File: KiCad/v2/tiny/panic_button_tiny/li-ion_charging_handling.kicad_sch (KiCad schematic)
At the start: 2 parts, among them U6 TP4056-42-ESOP8, U7 DW01A

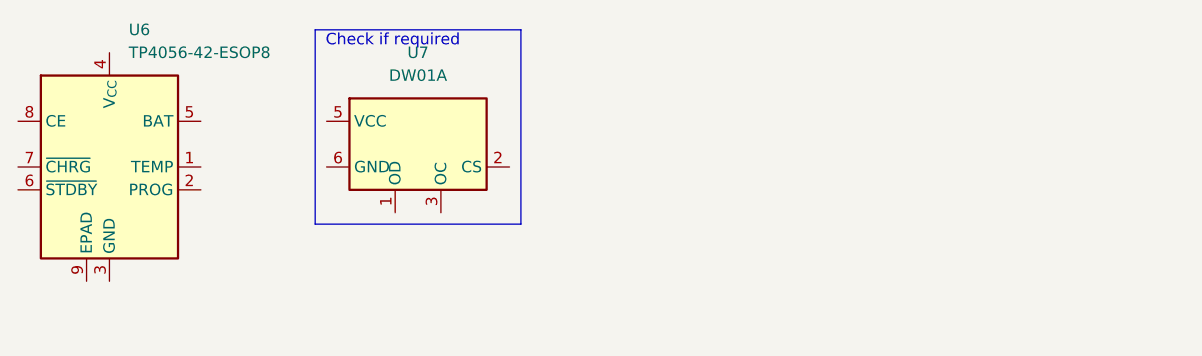
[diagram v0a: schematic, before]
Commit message: [UPDATE] the KiCad schematic to contain some of the updated designs for the circuit
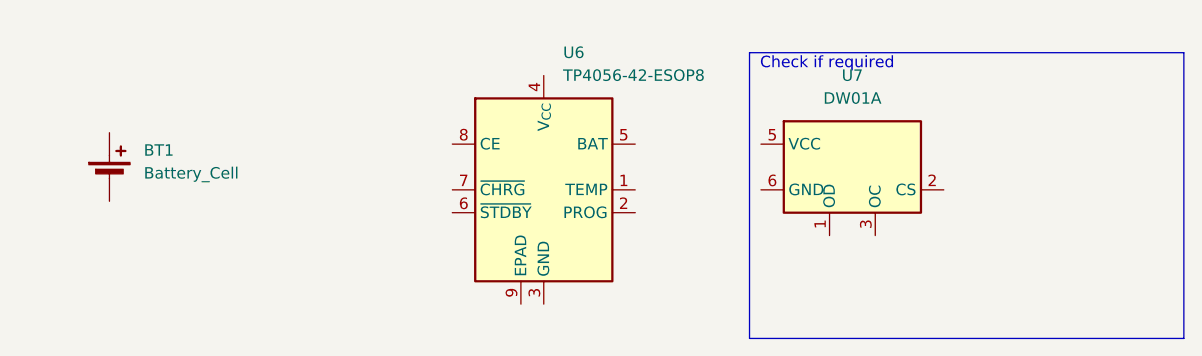
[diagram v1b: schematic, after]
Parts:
- added BT1: Battery_Cell, Connector_JST:JST_J2100_S06B-J21DK-GGXR_2x03_P2.50mm_Horizontal, symbol Device:Battery_Cell
- U7: footprint (none) -> Package_TO_SOT_SMD:SOT-23-6
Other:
- moved on the sheet: U6, U7
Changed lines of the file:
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@@
 	(paper "A4")
 	(rectangle
-		(start 55.88 15.24)
-		(end 78.74 36.83)
+		(start 104.14 17.78)
+		(end 152.4 49.53)
 		(stroke
 			(width 0)
@@
 	(text "Check if required"
 		(exclude_from_sim no)
-		(at 64.516 16.51 0)
+		(at 112.776 19.05 0)
 		(effects
 			(font
@@
 	(symbol
 		(lib_id "Battery_Management:DW01A")
-		(at 67.31 27.94 0)
+		(at 115.57 30.48 0)
 		(unit 1)
 		(body_style 1)
@@
 		(fields_autoplaced yes)
 		(property "Reference" "U7"
-			(at 67.31 17.78 0)
+			(at 115.57 20.32 0)
 			(show_name no)
 			(do_not_autoplace no)
@@
 		)
 		(property "Value" "DW01A"
-			(at 67.31 20.32 0)
-			(show_name no)
-			(do_not_autoplace no)
-			(effects
-				(font
-					(size 1.27 1.27)
-				)
-			)
-		)
-		(property "Footprint" ""
-			(at 67.31 27.94 0)
+			(at 115.57 22.86 0)
+			(show_name no)
+			(do_not_autoplace no)
+			(effects
+				(font
+					(size 1.27 1.27)
+				)
+			)
+		)
+		(property "Footprint" "Package_TO_SOT_SMD:SOT-23-6"
+			(at 115.57 30.48 0)
 			(hide yes)
 			(show_name no)
@@
 		)
 		(property "Datasheet" "https://hmsemi.com/downfile/DW01A.PDF"
-			(at 67.31 27.94 0)
+			(at 115.57 30.48 0)
 			(hide yes)
 			(show_name no)
@@
 		)
 		(property "Description" "Overcharge, overcurrent and overdischarge protection IC for single cell lithium-ion/polymer battery"
-			(at 67.564 26.416 0)
+			(at 115.824 28.956 0)
 			(hide yes)
 			(show_name no)
@@
 	)
 	(symbol
+		(lib_id "Device:Battery_Cell")
+		(at 33.02 31.75 0)
+		(unit 1)
+		(body_style 1)
+		(exclude_from_sim no)
+		(in_bom yes)
+		(on_board yes)
+		(in_pos_files yes)
+		(dnp no)
+		(fields_autoplaced yes)
+		(property "Reference" "BT1"
+			(at 36.83 28.6384 0)
+			(show_name no)
+			(do_not_autoplace no)
+			(effects
+				(font
+					(size 1.27 1.27)
+				)
+				(justify left)
+			)
+		)
+		(property "Value" "Battery_Cell"
+			(at 36.83 31.1784 0)
+			(show_name no)
+			(do_not_autoplace no)
+			(effects
+				(font
+					(size 1.27 1.27)
+				)
+				(justify left)
+			)
+		)
+		(property "Footprint" "Connector_JST:JST_J2100_S06B-J21DK-GGXR_2x03_P2.50mm_Horizontal"
+			(at 33.02 30.226 90)
+			(hide yes)
+			(show_name no)
+			(do_not_autoplace no)
+			(effects
+				(font
+					(size 1.27 1.27)
+				)
+			)
+		)
+		(property "Datasheet" ""
+			(at 33.02 30.226 90)
+			(hide yes)
+			(show_name no)
+			(do_not_autoplace no)
+			(effects
+				(font
+					(size 1.27 1.27)
+				)
+			)
+		)
+		(property "Description" "Single-cell battery"
+			(at 33.02 31.75 0)
+			(hide yes)
+			(show_name no)
+			(do_not_autoplace no)
+			(effects
+				(font
+					(size 1.27 1.27)
+				)
+			)
+		)
+		(property "Sim.Device" "V"
+			(at 33.02 31.75 0)
+			(hide yes)
+			(show_name no)
+			(do_not_autoplace no)
+			(effects
+				(font
+					(size 1.27 1.27)
+				)
+			)
+		)
+		(property "Sim.Type" "DC"
+			(at 33.02 31.75 0)
+			(hide yes)
+			(show_name no)
+			(do_not_autoplace no)
+			(effects
+				(font
+					(size 1.27 1.27)
+				)
+			)
+		)
+		(property "Sim.Pins" "1=+ 2=-"
+			(at 33.02 31.75 0)
+			(hide yes)
+			(show_name no)
+			(do_not_autoplace no)
+			(effects
+				(font
+					(size 1.27 1.27)
+				)
+			)
+		)
+		(pin "1"
+		)
+		(pin "2"
+		)
+		(instances
+			(project "panic_button_tiny"
+				(path "/c4eb92e9-b42f-4db0-b1d9-0ef70f7ca601/bf7d15b7-3a35-46fb-a5a6-5ea810f2dc2c/4988fc48-ac14-475f-a329-fd119eb80de7"
+					(reference "BT1")
+					(unit 1)
+				)
+			)
+		)
+	)
+	(symbol
 		(lib_id "Battery_Management:TP4056-42-ESOP8")
-		(at 33.02 30.48 0)
+		(at 81.28 33.02 0)
 		(unit 1)
 		(body_style 1)
@@
 		(fields_autoplaced yes)
 		(property "Reference" "U6"
-			(at 35.1633 15.24 0)
+			(at 83.4233 17.78 0)
 			(show_name no)
 			(do_not_autoplace no)
@@
 		)
 		(property "Value" "TP4056-42-ESOP8"
-			(at 35.1633 17.78 0)
+			(at 83.4233 20.32 0)
 			(show_name no)
 			(do_not_autoplace no)
@@
 		)
 		(property "Footprint" "Package_SO:SOIC-8-1EP_3.9x4.9mm_P1.27mm_EP2.41x3.3mm_ThermalVias"
-			(at 33.528 53.34 0)
+			(at 81.788 55.88 0)
 			(hide yes)
 			(show_name no)
@@
 		)
 		(property "Datasheet" "https://www.lcsc.com/datasheet/lcsc_datasheet_2410121619_TOPPOWER-Nanjing-Extension-Microelectronics-TP4056-42-ESOP8_C16581.pdf"
-			(at 33.02 55.88 0)
+			(at 81.28 58.42 0)
 			(hide yes)
 			(show_name no)
@@
 		)
 		(property "Description" "1A Standalone Linear Li-ion/LiPo single-cell battery charger, 4.2V ±1% charge voltage, VCC = 4.0..8.0V, SOIC-8 (SOP-8)"
-			(at 33.528 50.8 0)
-			(hide yes)
-			(show_name no)
+			(at 81.788 53.34 0)
+			(hide yes)
+			(show_name no)

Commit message: [UPDATE] some of the pcb design and layout
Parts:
- BT1: footprint Connector_JST:JST_J2100_S06B-J21DK-GGXR_2x03_P2.50mm_Horizontal -> Connector_JST:JST_EH_S2B-EH_1x02_P2.50mm_Horizontal
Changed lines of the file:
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@@
 			)
 		)
-		(property "Footprint" "Connector_JST:JST_J2100_S06B-J21DK-GGXR_2x03_P2.50mm_Horizontal"
+		(property "Footprint" "Connector_JST:JST_EH_S2B-EH_1x02_P2.50mm_Horizontal"
 			(at 33.02 30.226 90)
 			(hide yes)

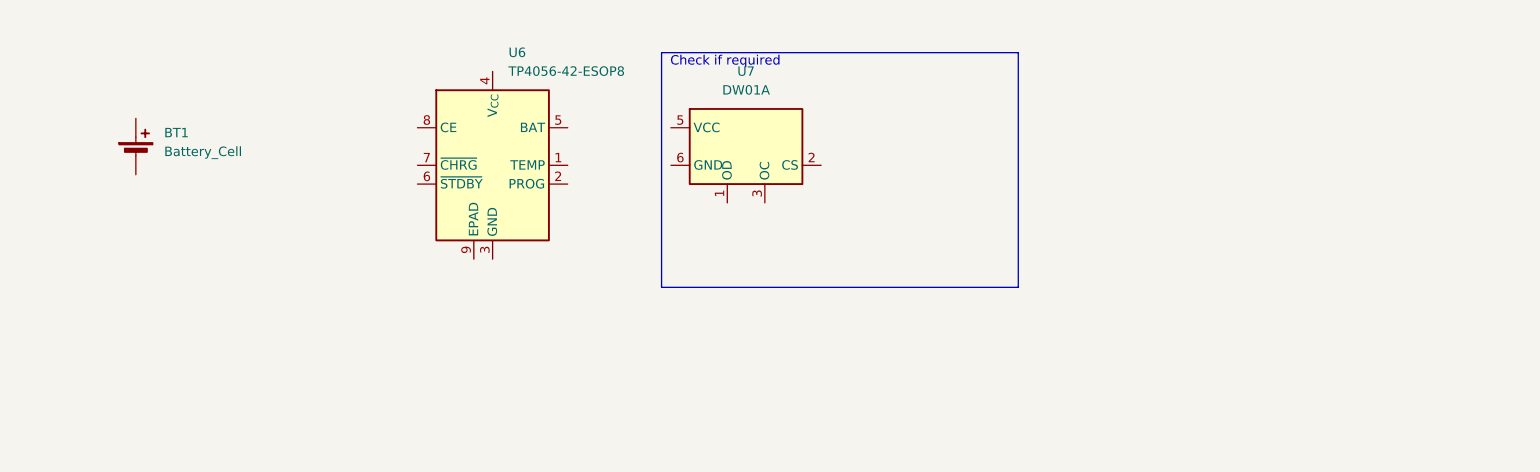
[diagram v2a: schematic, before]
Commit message: [UPDATE] connections in the circuit schematic
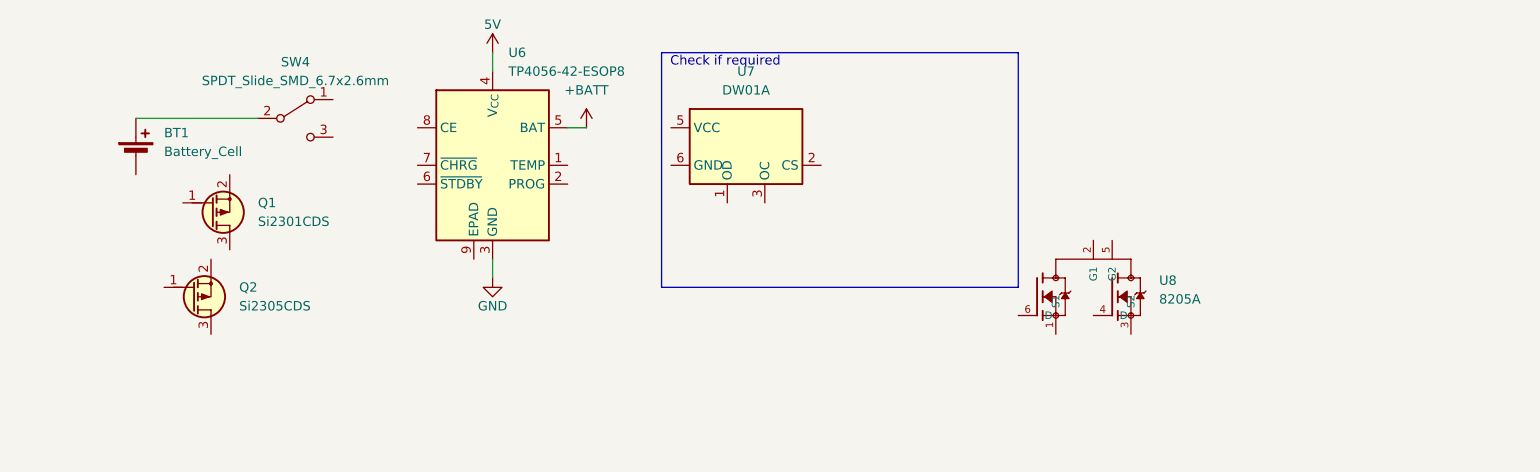
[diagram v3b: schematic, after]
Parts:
- added Q1: Si2301CDS, PCM_Package_TO_SOT_SMD_AKL:SOT-23, symbol PCM_Transistor_MOSFET_AKL:Si2301CDS
- added Q2: Si2305CDS, PCM_Package_TO_SOT_SMD_AKL:SOT-23, symbol PCM_Transistor_MOSFET_AKL:Si2305CDS
- added SW4: SPDT_Slide_SMD_6.7x2.6mm, PCM_SparkFun-Switch:Slide_SPST_SMD_6.7x2.6mm, symbol PCM_SparkFun-Switch:SPDT_Slide_SMD_6.7x2.6mm
- added U8: 8205A, 8205A:SOT95P285X140-6N, symbol 8205A:8205A
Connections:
- net at BT1.1 (+): now also SW4.2
- net GND: now reaches U6.3 (GND)
- net 5V: now reaches U6.4 (V_{CC})
- net +BATT: now reaches U6.5 (BAT)

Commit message: [UPDATE] connections in the circuits
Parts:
- added LED1: LED_1.8mm_SMD_Red, PCM_LED_SMD_AKL:LED_1.8mm_GullWing, symbol PCM_LED_AKL:LED_1.8mm_SMD_Red
- added LED2: LED_1.8mm_SMD_Green, PCM_LED_SMD_AKL:LED_1.8mm_GullWing, symbol PCM_LED_AKL:LED_1.8mm_SMD_Green
- added R6, R7: 1k_0603, PCM_Resistor_SMD_AKL:R_0603_1608Metric_Pad0.98x0.95mm_HandSolder, symbol PCM_4ms_Resistor:1k_0603
- added R8: 1.2k_0603, PCM_Resistor_SMD_AKL:R_0201_0603Metric_Pad0.64x0.40mm_HandSolder, symbol PCM_4ms_Resistor:1.2k_0603
- added R9: 10k_0603, PCM_Resistor_SMD_AKL:R_0603_1608Metric_Pad0.98x0.95mm_HandSolder, symbol PCM_4ms_Resistor:10k_0603
- added TP10, TP11, TP7, TP8: 1.25mm, TestPoint:TestPoint_2Pads_Pitch2.54mm_Drill0.8mm, symbol PCM_SparkFun-Connector:TestPoint_1.25mm
- added TP9: TestPoint, TestPoint:TestPoint_THTPad_D4.0mm_Drill2.0mm, symbol Connector:TestPoint
- renumbered Q2 to Q1, Q1 to Q2
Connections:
- net +BATT: now also Q1.3 (D), TP10.1
- net GND: now also BT1.2 (-), U6.9 (EPAD), U7.6 (GND), LED1.1 (K), LED2.1 (K), R8.2
- net at U7.1 (OD): now also U8.2 (G1)
- net at U7.2 (CS): now also U8.1 (S1), U8.3 (S2)
- net at U7.3 (OC): now also U8.4 (D)
- net at U7.5 (VCC): now also TP11.1
- net at SW4.1 (A): now also Q1.2 (S)
- net at U6.1 (TEMP): now also TP7.1
- net at U6.2 (PROG): now also R8.1
- net at U6.6 (~{STDBY}): now also R7.1
- net at U6.7 (~{CHRG}): now also R6.2
- net 3.3V: now reaches U6.8 (CE)
- new net: R9.2, TP9.1
- new net: LED2.2 (A), R7.2
- new net: LED1.2 (A), R6.1
- new net: R9.1, TP8.1
- no-connect marks 0 -> 1
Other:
- note added: "Onboard bms if not present in battery."
- note added: "Onboard bms toggle"
- note added: "Temperature Tracking If available"
- note removed: "Check if required"
- moved on the sheet: BT1, Q1, Q2, SW4, U6, U7, U8

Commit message: [UPDATE] the battery logic
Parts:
- removed Q2: Si2301CDS, PCM_Package_TO_SOT_SMD_AKL:SOT-23, symbol PCM_Transistor_MOSFET_AKL:Si2301CDS
- added TP12, TP13: 1.25mm, TestPoint:TestPoint_2Pads_Pitch2.54mm_Drill0.8mm, symbol PCM_SparkFun-Connector:TestPoint_1.25mm
- R8: value 1.2k_0603 -> 2.4k_0603; Display 1.2k -> 2.4k; Part Number RC0603FR-071K2L -> RC0603FR-072K4L; Specifications 1K2, 1%, 1/10W, 0603 -> 2K4, 1%, 1/10W, 0603
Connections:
- net +BATT: no longer TP10.1
- net GND: no longer BT1.2 (-), U7.6 (GND)
- net at U8.2: now also U7.6 (GND); no longer U7.1 (OD)
- net at BT1.1 (+): now also TP10.1; no longer SW4.2
- net at U8.5: now also TP13.1
- net at U8.6: now also U7.1 (OD)
- net -BATT: now reaches Q1.1 (G)
- new net: BT1.2 (-), TP12.1
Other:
- note added: "Charging regulator"
- note added: "negative"
- note added: "positive"
- moved on the sheet: LED1, LED2, Q1, R6, R7, R8, R9, SW4, TP7, TP8, TP9, U6
